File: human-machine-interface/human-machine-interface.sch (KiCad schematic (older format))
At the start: 25 parts, among them J1 Conn_01x04_Male, J2 Conn_01x04_Male, J3 Conn_01x04_Male, J4 Conn_01x04_Male, J5 5.4mm/2.5mm, SW1 SW_Push, SW2 SW_Push, SW3 SW_DPDT_x2, U1 NRF24L01+, U2 Teensy3.2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

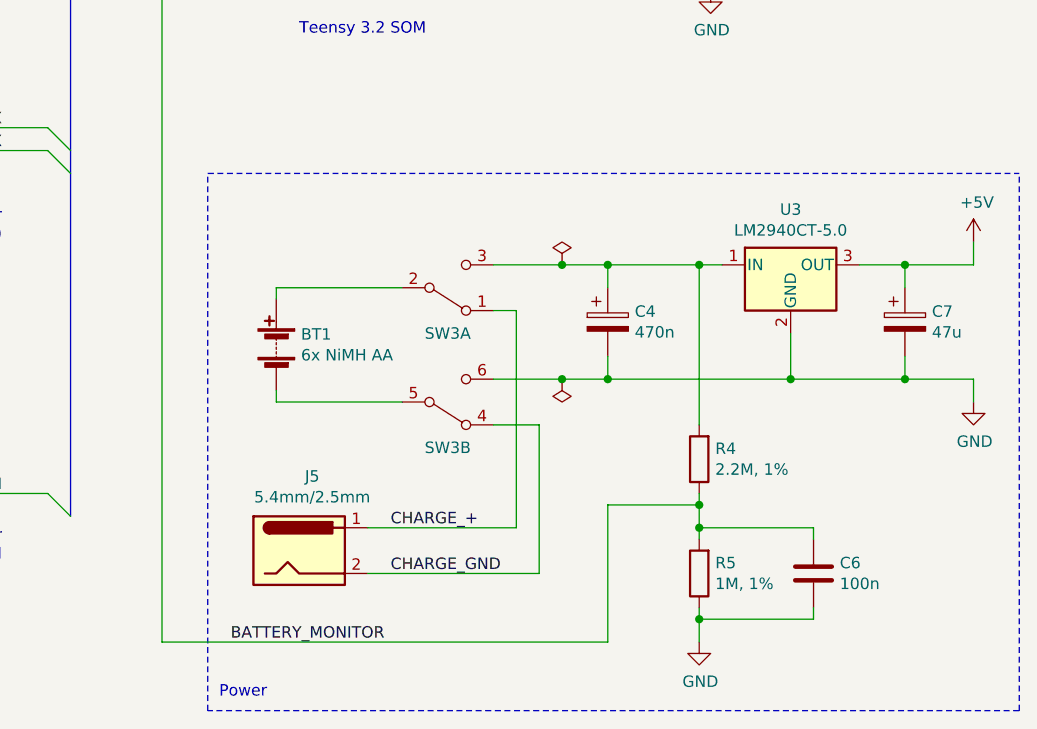
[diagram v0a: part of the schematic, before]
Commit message: Add diode to HMI's charge port
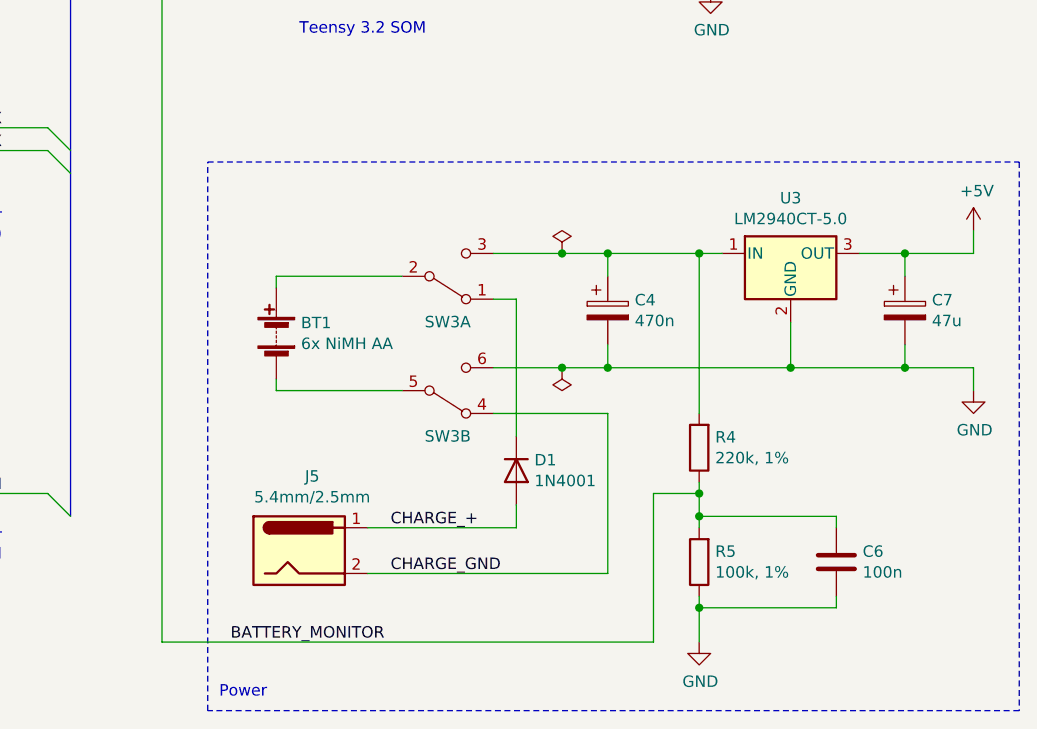
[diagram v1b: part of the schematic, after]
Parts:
- added D1: 1N4001, Diode_THT:D_DO-41_SOD81_P10.16mm_Horizontal, symbol Diode:1N4001
- R4: value 2.2M, 1% -> 220k, 1%
- R5: value 1M, 1% -> 100k, 1%
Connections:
- net CHARGE_+: now also D1.2 (A); no longer SW3.1 (A)
- new net: D1.1 (K), SW3.1 (A)
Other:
- moved on the sheet: BT1, C4, C6, C7, R4, R5, SW3A, SW3B, U3

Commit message: Route HMI PCB
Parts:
- BT1, J5, JP1, SW1, SW2: footprint (none) -> Connector_PinHeader_2.54mm:PinHeader_1x02_P2.54mm_Vertical
- C1, C2, C3, C5, C7: footprint (none) -> Capacitor_THT:CP_Radial_D5.0mm_P2.50mm
- C4, C6: footprint (none) -> Capacitor_THT:C_Rect_L10.0mm_W5.0mm_P5.00mm_P7.50mm
- J1, J2, J3, J4: footprint (none) -> Connector_PinHeader_2.54mm:PinHeader_1x04_P2.54mm_Vertical
- R1, R2, R3, R4, R5: footprint (none) -> Resistor_THT:R_Axial_DIN0207_L6.3mm_D2.5mm_P10.16mm_Horizontal
- SW3: footprint (none) -> earth-rover-footprints:PinHeader_2x03_P2.54mm_Vertical_Switch_DPDT
- U2: footprint (none) -> earth-rover-footprints:Teensy_3.2
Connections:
- net +3V3: now also C3.1, J2.2 (Pin_2)
- net +5V: no longer C3.1, J2.1 (Pin_1)
- net CHARGE_GND: now also SW3.1 (A); no longer SW3.4 (A)
- net GND: now also J2.1 (Pin_1), SW3.3 (C); no longer J2.4 (Pin_4), SW3.6 (C)
- net GPS_SERIAL_RX: now also J2.4 (Pin_4); no longer J2.3 (Pin_3)
- net GPS_SERIAL_TX: now also J2.3 (Pin_3); no longer J2.2 (Pin_2)
- net at D1.1 (K): now also SW3.4 (A); no longer SW3.1 (A)
- net BATT_+: now reaches BT1.1 (+)
- net BATT_+: now also SW3.5 (B); no longer SW3.2 (B)
- net at C4.1, R4.2, U3.1 (IN): now also SW3.6 (C); no longer SW3.3 (C)
- net BATT_GND: now reaches BT1.2 (-)
- net BATT_GND: now also SW3.2 (B); no longer SW3.5 (B)
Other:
- moved on the sheet: SW3A, SW3B
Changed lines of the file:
@@
 Sheet 1 1
 Title "Earth Rover"
-Date "2020-02-23"
-Rev "8"
+Date "2020-06-11"
+Rev "9"
 Comp "Vijfendertig BVBA"
 Comment1 "Maarten De Munck"
@@
 F 3 "" H 2050 7800 50  0001 C CNN
 	1    2050 7800
-	1    0    0    -1
-$EndComp
-$Comp
-L power:+5V #PWR012
-U 1 1 5E01812E
-P 2050 7300
-F 0 "#PWR012" H 2050 7150 50  0001 C CNN
-F 1 "+5V" H 2065 7473 50  0000 C CNN
-F 2 "" H 2050 7300 50  0001 C CNN
-F 3 "" H 2050 7300 50  0001 C CNN
-	1    2050 7300
 	1    0    0    -1
 $EndComp
@@
 L Switch:SW_DPDT_x2 SW3
 U 2 1 5DDAD789
+P 5150 8150
+F 0 "SW3" H 5150 8350 50  0000 C CNN
+F 1 "SW_DPDT_x2" H 5150 8344 50  0001 C CNN
+F 2 "earth-rover-footprints:PinHeader_2x03_P2.54mm_Vertical_Switch_DPDT" H 5150 8150 50  0001 C CNN
+F 3 "~" H 5150 8150 50  0001 C CNN
+	2    5150 8150
+	1    0    0    1
+$EndComp
+$Comp
+L Switch:SW_DPDT_x2 SW3
+U 1 1 5DDAD09C
 P 5150 8650
 F 0 "SW3" H 5150 8850 50  0000 C CNN
 F 1 "SW_DPDT_x2" H 5150 8844 50  0001 C CNN
-F 2 "" H 5150 8650 50  0001 C CNN
+F 2 "earth-rover-footprints:PinHeader_2x03_P2.54mm_Vertical_Switch_DPDT" H 5150 8650 50  0001 C CNN
 F 3 "~" H 5150 8650 50  0001 C CNN
-	2    5150 8650
-	1    0    0    1
-$EndComp
-$Comp
-L Switch:SW_DPDT_x2 SW3
-U 1 1 5DDAD09C
-P 5150 8150
-F 0 "SW3" H 5150 8350 50  0000 C CNN
-F 1 "SW_DPDT_x2" H 5150 8344 50  0001 C CNN
-F 2 "" H 5150 8150 50  0001 C CNN
-F 3 "~" H 5150 8150 50  0001 C CNN
-	1    5150 8150
+	1    5150 8650
 	1    0    0    1
 $EndComp
@@
 F 0 "JP1" H 1700 9335 50  0000 C CNN
 F 1 "Jumper_2_Open" H 1700 9244 50  0000 C CNN
-F 2 "" H 1700 9100 50  0001 C CNN
+F 2 "Connector_PinHeader_2.54mm:PinHeader_1x02_P2.54mm_Vertical" H 1700 9100 50  0001 C CNN
 F 3 "~" H 1700 9100 50  0001 C CNN
 	1    1700 9100
@@
 F 0 "R2" H 2270 8896 50  0000 L CNN
 F 1 "10k" H 2270 8805 50  0000 L CNN
-F 2 "" V 2130 8850 50  0001 C CNN
+F 2 "Resistor_THT:R_Axial_DIN0207_L6.3mm_D2.5mm_P10.16mm_Horizontal" V 2130 8850 50  0001 C CNN
 F 3 "~" H 2200 8850 50  0001 C CNN
 	1    2200 8850
@@
 F 0 "C2" H 1468 5846 50  0000 L CNN
 F 1 "10u" H 1468 5755 50  0000 L CNN
-F 2 "" H 1350 5800 50  0001 C CNN
+F 2 "Capacitor_THT:CP_Radial_D5.0mm_P2.50mm" H 1350 5800 50  0001 C CNN
 F 3 "~" H 1350 5800 50  0001 C CNN
 	1    1350 5800
@@
 F 0 "SW1" H 1700 1835 50  0000 C CNN
 F 1 "SW_Push" H 1700 1744 50  0000 C CNN
-F 2 "" H 1700 1750 50  0001 C CNN
+F 2 "Connector_PinHeader_2.54mm:PinHeader_1x02_P2.54mm_Vertical" H 1700 1750 50  0001 C CNN
 F 3 "~" H 1700 1750 50  0001 C CNN
 	1    1700 1550
@@
 F 0 "R1" H 2070 1296 50  0000 L CNN
 F 1 "10k" H 2070 1205 50  0000 L CNN
-F 2 "" V 1930 1250 50  0001 C CNN
+F 2 "Resistor_THT:R_Axial_DIN0207_L6.3mm_D2.5mm_P10.16mm_Horizontal" V 1930 1250 50  0001 C CNN
 F 3 "~" H 2000 1250 50  0001 C CNN
 	1    2000 1250
@@
 F 0 "R3" H 4120 1296 50  0000 L CNN
 F 1 "10k" H 4120 1205 50  0000 L CNN
-F 2 "" V 3980 1250 50  0001 C CNN
+F 2 "Resistor_THT:R_Axial_DIN0207_L6.3mm_D2.5mm_P10.16mm_Horizontal" V 3980 1250 50  0001 C CNN
 F 3 "~" H 4050 1250 50  0001 C CNN
 	1    4050 1250
@@
 F 0 "SW2" H 3750 1835 50  0000 C CNN
 F 1 "SW_Push" H 3750 1744 50  0000 C CNN
-F 2 "" H 3750 1750 50  0001 C CNN
+F 2 "Connector_PinHeader_2.54mm:PinHeader_1x02_P2.54mm_Vertical" H 3750 1750 50  0001 C CNN
 F 3 "~" H 3750 1750 50  0001 C CNN
 	1    3750 1550
@@
 F 0 "C3" H 1468 7596 50  0000 L CNN
 F 1 "10u" H 1468 7505 50  0000 L CNN
-F 2 "" H 1388 7400 50  0001 C CNN
+F 2 "Capacitor_THT:CP_Radial_D5.0mm_P2.50mm" H 1388 7400 50  0001 C CNN
 F 3 "~" H 1350 7550 50  0001 C CNN
 	1    1350 7550
@@
 $EndComp
 Wire Wire Line
-	2050 7300 2050 7400
-Wire Wire Line
-	2050 7700 2050 7800
-$Comp
-L power:+5V #PWR04
-U 1 1 5E0B9488
-P 1350 7300
-F 0 "#PWR04" H 1350 7150 50  0001 C CNN
-F 1 "+5V" H 1365 7473 50  0000 C CNN
-F 2 "" H 1350 7300 50  0001 C CNN
-F 3 "" H 1350 7300 50  0001 C CNN
-	1    1350 7300
-	1    0    0    -1
-$EndComp
+	2150 7300 2150 7500
+Wire Wire Line
+	2050 7400 2050 7800
 $Comp
 L power:GND #PWR05
@@
 F 0 "C5" H 6618 5846 50  0000 L CNN
 F 1 "10u" H 6618 5755 50  0000 L CNN
-F 2 "" H 6538 5650 50  0001 C CNN
+F 2 "Capacitor_THT:CP_Radial_D5.0mm_P2.50mm" H 6538 5650 50  0001 C CNN
 F 3 "~" H 6500 5800 50  0001 C CNN
 	1    6500 5800
@@
 F 0 "U2" H 5300 4287 60  0000 C CNN
 F 1 "Teensy3.2" H 5300 4181 60  0000 C CNN
-F 2 "" H 8100 2850 60  0001 C CNN
+F 2 "earth-rover-footprints:Teensy_3.2" H 8100 2850 60  0001 C CNN
 F 3 "" H 8100 2850 60  0000 C CNN
 	1    4700 4000
@@
 F 0 "J1" H 1900 4250 50  0000 R CNN
 F 1 "Conn_01x04_Male" H 1950 3650 50  0001 R CNN
-F 2 "" H 1750 4000 50  0001 C CNN
+F 2 "Connector_PinHeader_2.54mm:PinHeader_1x04_P2.54mm_Vertical" H 1750 4000 50  0001 C CNN
 F 3 "~" H 1750 4000 50  0001 C CNN
 	1    1750 4000
@@
 F 0 "C1" H 1468 4096 50  0000 L CNN
 F 1 "10u" H 1468 4005 50  0000 L CNN
-F 2 "" H 1388 3900 50  0001 C CNN
+F 2 "Capacitor_THT:CP_Radial_D5.0mm_P2.50mm" H 1388 3900 50  0001 C CNN
 F 3 "~" H 1350 4050 50  0001 C CNN
 	1    1350 4050
@@
 Text Label 3200 9100 2    50   ~ 0
 RESET_EEPROM
-Text Label 3200 7600 2    50   ~ 0
+Text Label 3200 7700 2    50   ~ 0
 GPS_SERIAL_RX
 Text Label 3200 4000 2    50   ~ 0
@@
 	2500 6100 3400 6100
 Wire Wire Line
-	1950 7700 2050 7700
-Wire Wire Line
 	1950 7400 2050 7400
-Text Label 3200 7500 2    50   ~ 0
+Wire Wire Line
+	1950 7500 2150 7500
+Text Label 3200 7600 2    50   ~ 0
 GPS_SERIAL_TX
 $Comp
@@
 F 0 "J2" H 1900 7750 50  0000 R CNN
 F 1 "Conn_01x04_Male" H 1950 7150 50  0001 R CNN
-F 2 "" H 1750 7500 50  0001 C CNN
+F 2 "Connector_PinHeader_2.54mm:PinHeader_1x04_P2.54mm_Vertical" H 1750 7500 50  0001 C CNN
 F 3 "~" H 1750 7500 50  0001 C CNN
 	1    1750 7500
 	1    0    0    -1
 $EndComp
-Wire Wire Line
-	1950 7500 3400 7500
-Wire Wire Line
-	1950 7600 3400 7600
+Entry Wire Line
+	3400 7700 3500 7800
 Entry Wire Line
 	3400 7600 3500 7700
-Entry Wire Line
-	3400 7500 3500 7600
 Wire Wire Line
 	1950 4100 3400 4100
@@
 F 0 "J3" H 1950 2650 50  0000 C CNN
 F 1 "Conn_01x04_Male" H 1958 2590 50  0001 C CNN
-F 2 "" H 1850 2400 50  0001 C CNN
+F 2 "Connector_PinHeader_2.54mm:PinHeader_1x04_P2.54mm_Vertical" H 1850 2400 50  0001 C CNN
 F 3 "~" H 1850 2400 50  0001 C CNN
 	1    1850 2400
@@
 F 0 "J4" H 4000 2650 50  0000 C CNN
 F 1 "Conn_01x04_Male" H 4008 2590 50  0001 C CNN
-F 2 "" H 3900 2400 50  0001 C CNN
+F 2 "Connector_PinHeader_2.54mm:PinHeader_1x04_P2.54mm_Vertical" H 3900 2400 50  0001 C CNN
 F 3 "~" H 3900 2400 50  0001 C CNN
 	1    3900 2400
@@
 F 0 "J5" H 4557 9675 50  0000 C CNN
 F 1 "5.4mm/2.5mm" H 4557 9584 50  0000 C CNN
-F 2 "" H 4550 9310 50  0001 C CNN
+F 2 "Connector_PinHeader_2.54mm:PinHeader_1x02_P2.54mm_Vertical" H 4550 9310 50  0001 C CNN
 F 3 "~" H 4550 9310 50  0001 C CNN
 	1    4500 9350
@@
 F 0 "C7" H 7268 8346 50  0000 L CNN
 F 1 "47u" H 7268 8255 50  0000 L CNN
-F 2 "" H 7188 8150 50  0001 C CNN
+F 2 "Capacitor_THT:CP_Radial_D5.0mm_P2.50mm" H 7188 8150 50  0001 C CNN
 F 3 "~" H 7150 8300 50  0001 C CNN
 	1    7150 8300
@@
 F 0 "C4" H 5968 8346 50  0000 L CNN
 F 1 "470n" H 5968 8255 50  0000 L CNN
-F 2 "" H 5888 8150 50  0001 C CNN
+F 2 "Capacitor_THT:C_Rect_L10.0mm_W5.0mm_P5.00mm_P7.50mm" H 5888 8150 50  0001 C CNN
 F 3 "~" H 5850 8300 50  0001 C CNN
 	1    5850 8300
@@
 F 0 "R4" H 6180 8854 50  0000 R CNN
 F 1 "220k, 1%" H 6180 8945 50  0000 R CNN
-F 2 "" V 6180 8900 50  0001 C CNN
+F 2 "Resistor_THT:R_Axial_DIN0207_L6.3mm_D2.5mm_P10.16mm_Horizontal" V 6180 8900 50  0001 C CNN
 F 3 "~" H 6250 8900 50  0001 C CNN
 	1    6250 8900
@@
 F 0 "R5" H 6180 9354 50  0000 R CNN
 F 1 "100k, 1%" H 6180 9445 50  0000 R CNN
-F 2 "" V 6180 9400 50  0001 C CNN
+F 2 "Resistor_THT:R_Axial_DIN0207_L6.3mm_D2.5mm_P10.16mm_Horizontal" V 6180 9400 50  0001 C CNN
 F 3 "~" H 6250 9400 50  0001 C CNN
 	1    6250 9400
@@
 F 0 "C6" H 6965 9446 50  0000 L CNN
 F 1 "100n" H 6965 9355 50  0000 L CNN
-F 2 "" H 6888 9250 50  0001 C CNN
+F 2 "Capacitor_THT:C_Rect_L10.0mm_W5.0mm_P5.00mm_P7.50mm" H 6888 9250 50  0001 C CNN
 F 3 "~" H 6850 9400 50  0001 C CNN
 	1    6850 9400
@@
 F 0 "BT1" H 4292 8446 50  0000 R CNN
 F 1 "6x NiMH AA" H 4292 8355 50  0000 R CNN
-F 2 "" V 4400 8460 50  0001 C CNN
+F 2 "Connector_PinHeader_2.54mm:PinHeader_1x02_P2.54mm_Vertical" V 4400 8460 50  0001 C CNN
 F 3 "~" V 4400 8460 50  0001 C CNN
 	1    4400 8400
@@
 Wire Notes Line
 	7650 7650 7650 10050
+Text Label 4500 8150 0    50   ~ 0
+BATT_+
+Text Label 4500 8650 0    50   ~ 0
+BATT_GND
+$Comp
+L power:+3.3V #PWR?
+U 1 1 5EE7CBBF
+P 1350 7300
+F 0 "#PWR?" H 1350 7150 50  0001 C CNN
+F 1 "+3.3V" H 1365 7473 50  0000 C CNN
+F 2 "" H 1350 7300 50  0001 C CNN
+F 3 "" H 1350 7300 50  0001 C CNN
+	1    1350 7300
+	1    0    0    -1
+$EndComp
+$Comp
+L power:+3.3V #PWR?
+U 1 1 5EE82182
+P 2150 7300
+F 0 "#PWR?" H 2150 7150 50  0001 C CNN
+F 1 "+3.3V" H 2165 7473 50  0000 C CNN
+F 2 "" H 2150 7300 50  0001 C CNN
+F 3 "" H 2150 7300 50  0001 C CNN
+	1    2150 7300
+	1    0    0    -1
+$EndComp
+Wire Wire Line
+	3400 7600 1950 7600
+Wire Wire Line
+	1950 7700 3400 7700
 Wire Bus Line
 	2950 3300 3500 3300

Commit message: Use larger holes for nRF24L01+ breakout board
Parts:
- U1: footprint RF_Module:nRF24L01_Breakout -> earth-rover-footprints:nRF24L01_Breakout_LargerHoles
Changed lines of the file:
@@
 F 0 "U1" H 1950 6300 50  0000 R BNN
 F 1 "NRF24L01+" H 1950 5300 50  0000 R TNN
-F 2 "RF_Module:nRF24L01_Breakout" H 2150 6400 50  0001 L CIN
+F 2 "earth-rover-footprints:nRF24L01_Breakout_LargerHoles" H 2150 6400 50  0001 L CIN
 F 3 "http://www.nordicsemi.com/eng/content/download/2730/34105/file/nRF24L01_Product_Specification_v2_0.pdf" H 2000 5700 50  0001 C CNN
 	1    2000 5800
@@
 BATT_GND
 $Comp
-L power:+3.3V #PWR?
+L power:+3.3V #PWR0101
 U 1 1 5EE7CBBF
 P 1350 7300
-F 0 "#PWR?" H 1350 7150 50  0001 C CNN
+F 0 "#PWR0101" H 1350 7150 50  0001 C CNN
 F 1 "+3.3V" H 1365 7473 50  0000 C CNN
 F 2 "" H 1350 7300 50  0001 C CNN
@@
 $EndComp
 $Comp
-L power:+3.3V #PWR?
+L power:+3.3V #PWR0102
 U 1 1 5EE82182
 P 2150 7300
-F 0 "#PWR?" H 2150 7150 50  0001 C CNN
+F 0 "#PWR0102" H 2150 7150 50  0001 C CNN
 F 1 "+3.3V" H 2165 7473 50  0000 C CNN
 F 2 "" H 2150 7300 50  0001 C CNN
